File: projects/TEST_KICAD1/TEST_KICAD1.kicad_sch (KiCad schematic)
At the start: 5 parts, among them U1 ATmega328P-A, Y1 Crystal

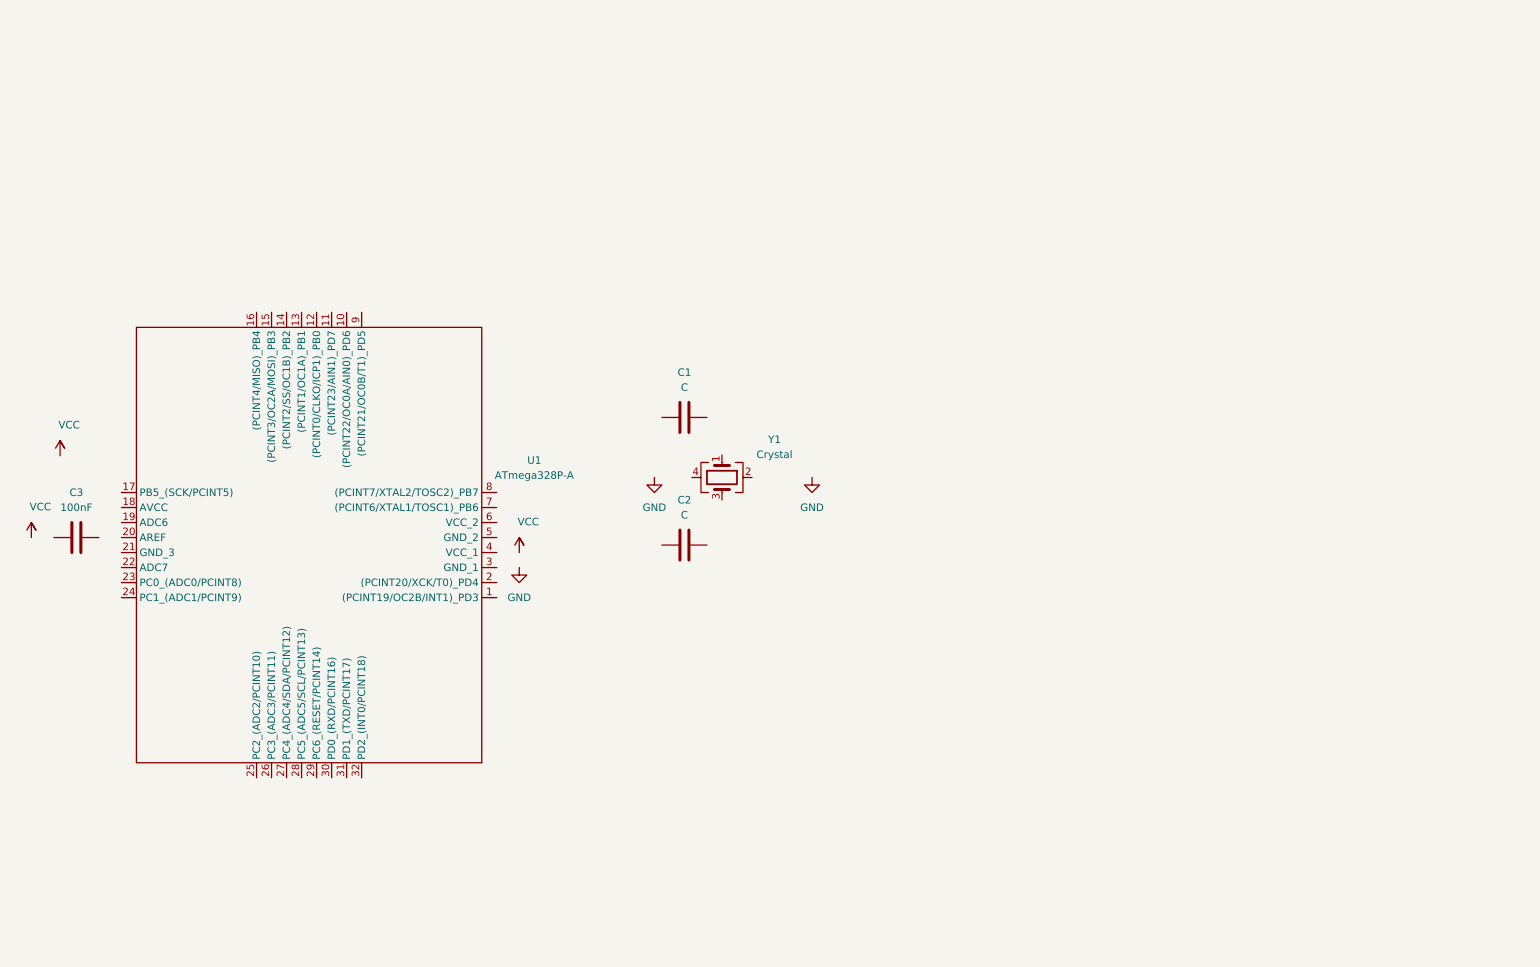
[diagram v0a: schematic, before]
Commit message: creation schematics, ajout power_flag, premier test erc
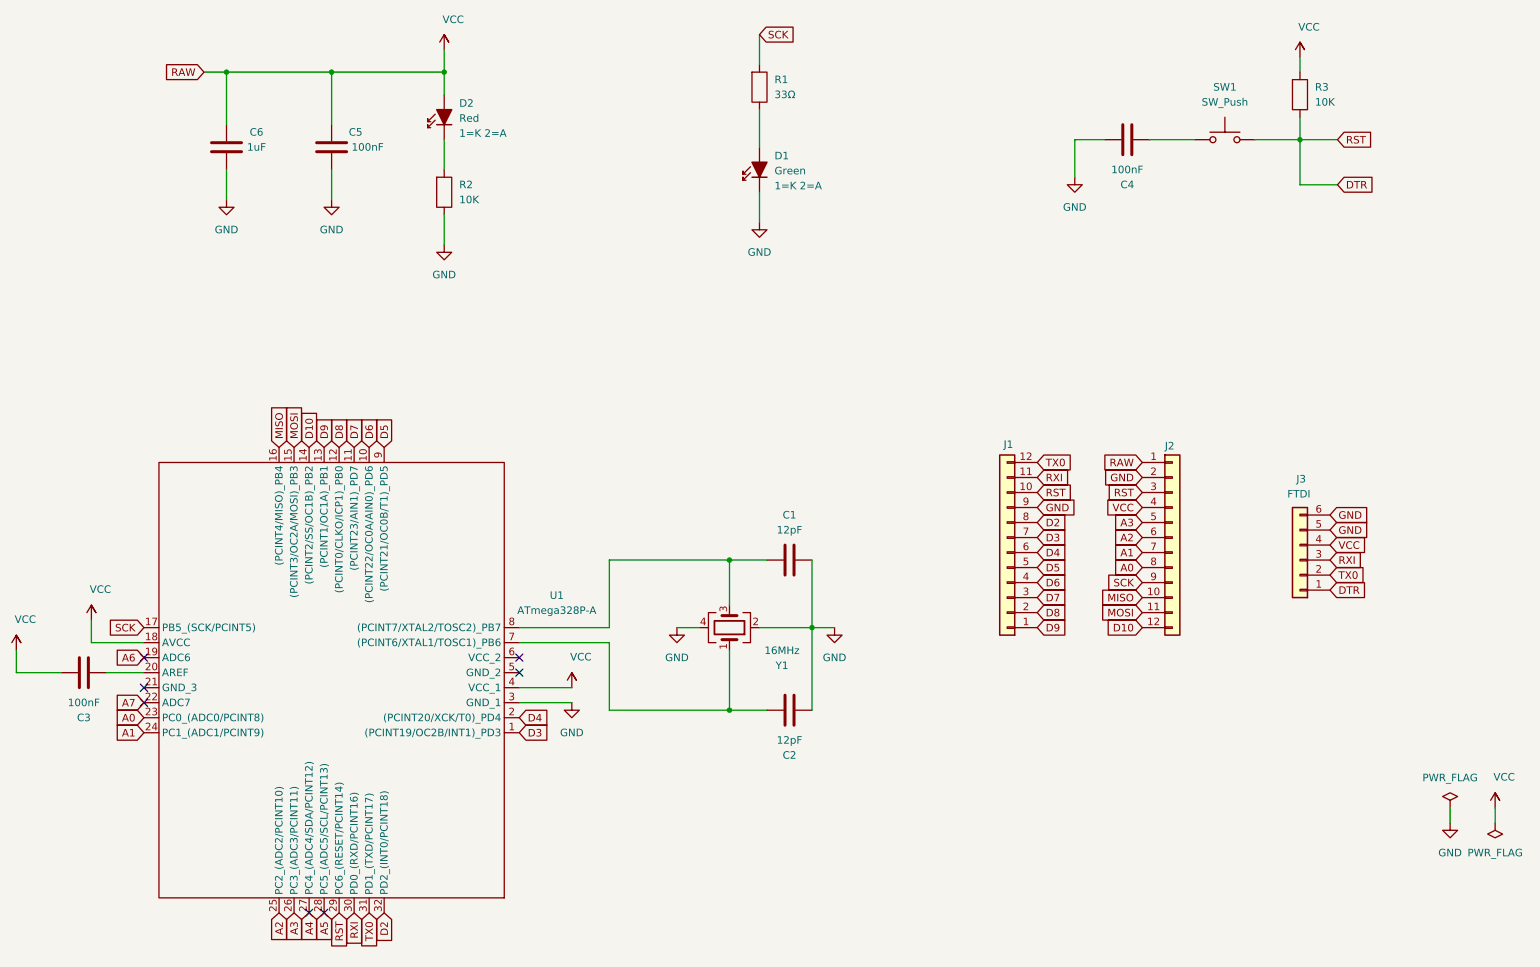
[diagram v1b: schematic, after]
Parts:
- added C4, C5: 100nF, symbol New_Library:C
- added C6: 1uF, symbol New_Library:C
- added D1: Green, symbol New_Library:LED
- added D2: Red, symbol New_Library:LED
- added J1, J2: ~, symbol New_Library:J
- added J3: FTDI, symbol New_Library:J_FTDI
- added R1: 33Ω, symbol New_Library:R
- added R2, R3: 10K, symbol New_Library:R
- added SW1: SW_Push, symbol New_Library:SW_Push
- C1, C2: value C -> 12pF
- Y1: value Crystal -> 16MHz
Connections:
- net GND: now also C1.2, C2.2, U1.3 (GND_1), Y1.2, Y1.4, C4.2, C5.1, C6.2, D1.2 (A), J1.9 (Pin_9), J2.2 (Pin_2), J3.5 (Pin_5), J3.6 (Pin_6), R2.2
- net VCC: now also C3.1, U1.18 (AVCC), U1.4 (VCC_1), C5.2, C6.1, D2.1 (K), J2.1 (Pin_1), J2.4 (Pin_4), J3.4 (Pin_4), R3.1
- net at C1.1: now also U1.8 ((PCINT7/XTAL2/TOSC2)_PB7), Y1.3
- net at Y1.1: now also C2.1, U1.7 ((PCINT6/XTAL1/TOSC1)_PB6)
- net at C3.2: now also U1.20 (AREF)
- net D3: now reaches U1.1 ((PCINT19/OC2B/INT1)_PD3)
- net D3: now also J1.7 (Pin_7)
- net D6: now reaches U1.10 ((PCINT22/OC0A/AIN0)_PD6)
- net D6: now also J1.4 (Pin_4)
- net D7: now reaches U1.11 ((PCINT23/AIN1)_PD7)
- net D7: now also J1.3 (Pin_3)
- net D8: now reaches U1.12 ((PCINT0/CLKO/ICP1)_PB0)
- net D8: now also J1.2 (Pin_2)
- net D9: now reaches U1.13 ((PCINT1/OC1A)_PB1)
- net D9: now also J1.1 (Pin_1)
- net D10: now reaches U1.14 ((PCINT2/SS/OC1B)_PB2)
- net D10: now also J2.12 (Pin_12)
- net MOSI: now reaches U1.15 ((PCINT3/OC2A/MOSI)_PB3)
- net MOSI: now also J2.11 (Pin_11)
- net MISO: now reaches U1.16 ((PCINT4/MISO)_PB4)
- net MISO: now also J2.10 (Pin_10)
- net SCK: now reaches U1.17 (PB5_(SCK/PCINT5))
- net SCK: now also J2.9 (Pin_9), R1.1
- net A6: now reaches U1.19 (ADC6)
- net D4: now reaches U1.2 ((PCINT20/XCK/T0)_PD4)
- net D4: now also J1.6 (Pin_6)
- net A7: now reaches U1.22 (ADC7)
- net A0: now reaches U1.23 (PC0_(ADC0/PCINT8))
- net A0: now also J2.8 (Pin_8)
- net A1: now reaches U1.24 (PC1_(ADC1/PCINT9))
- net A1: now also J2.7 (Pin_7)
- net A2: now reaches U1.25 (PC2_(ADC2/PCINT10))
- net A2: now also J2.6 (Pin_6)
- net A3: now reaches U1.26 (PC3_(ADC3/PCINT11))
- net A3: now also J2.5 (Pin_5)
- net A4: now reaches U1.27 (PC4_(ADC4/SDA/PCINT12))
- net A5: now reaches U1.28 (PC5_(ADC5/SCL/PCINT13))
- net DTR: now reaches U1.29 (PC6_(RESET/PCINT14))
- net DTR: now also J1.10 (Pin_10), J2.3 (Pin_3), J3.1 (Pin_1), R3.2, SW1.1
- net RXI: now reaches U1.30 (PD0_(RXD/PCINT16))
- net RXI: now also J1.11 (Pin_11), J3.3 (Pin_3)
- net TX0: now reaches U1.31 (PD1_(TXD/PCINT17))
- net TX0: now also J1.12 (Pin_12), J3.2 (Pin_2)
- net D2: now reaches U1.32 (PD2_(INT0/PCINT18))
- net D2: now also J1.8 (Pin_8)
- net D5: now reaches U1.9 ((PCINT21/OC0B/T1)_PD5)
- net D5: now also J1.5 (Pin_5)
- new net: D2.2 (A), R2.1
- new net: C4.1, SW1.2
- new net: D1.1 (K), R1.2
- no-connect marks 0 -> 7
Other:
- moved on the sheet: C1, C2, C3, U1, Y1
